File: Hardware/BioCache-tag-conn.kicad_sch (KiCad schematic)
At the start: 36 parts, among them J1 Conn_01x16_Male, J10 Conn_01x04_Male, J11 Conn_01x05_Male, J12 Conn_01x04_Male, J13 Conn_01x01_Male, J14 Conn_01x02_Male, J15 Conn_01x01_Male, J16 Conn_01x01_Male, J17 Conn_01x01_Male, J18 Conn_01x01_Male, J19 Conn_01x02_Male, J2 Conn_01x16_Male, J20 Conn_01x02_Male, J21 Conn_01x02_Male, J22 Conn_01x01_Male, J23 Conn_01x01_Male, J24 Conn_01x01_Male, J25 Conn_01x01_Male, J3 Conn_01x14_Male, J4 Conn_01x14_Male, J5 Conn_01x04_Male, J6 Conn_01x05_Male, J7 Conn_01x05_Male, J8 Conn_01x04_Male, J9 Conn_01x05_Male, U9 61C1024

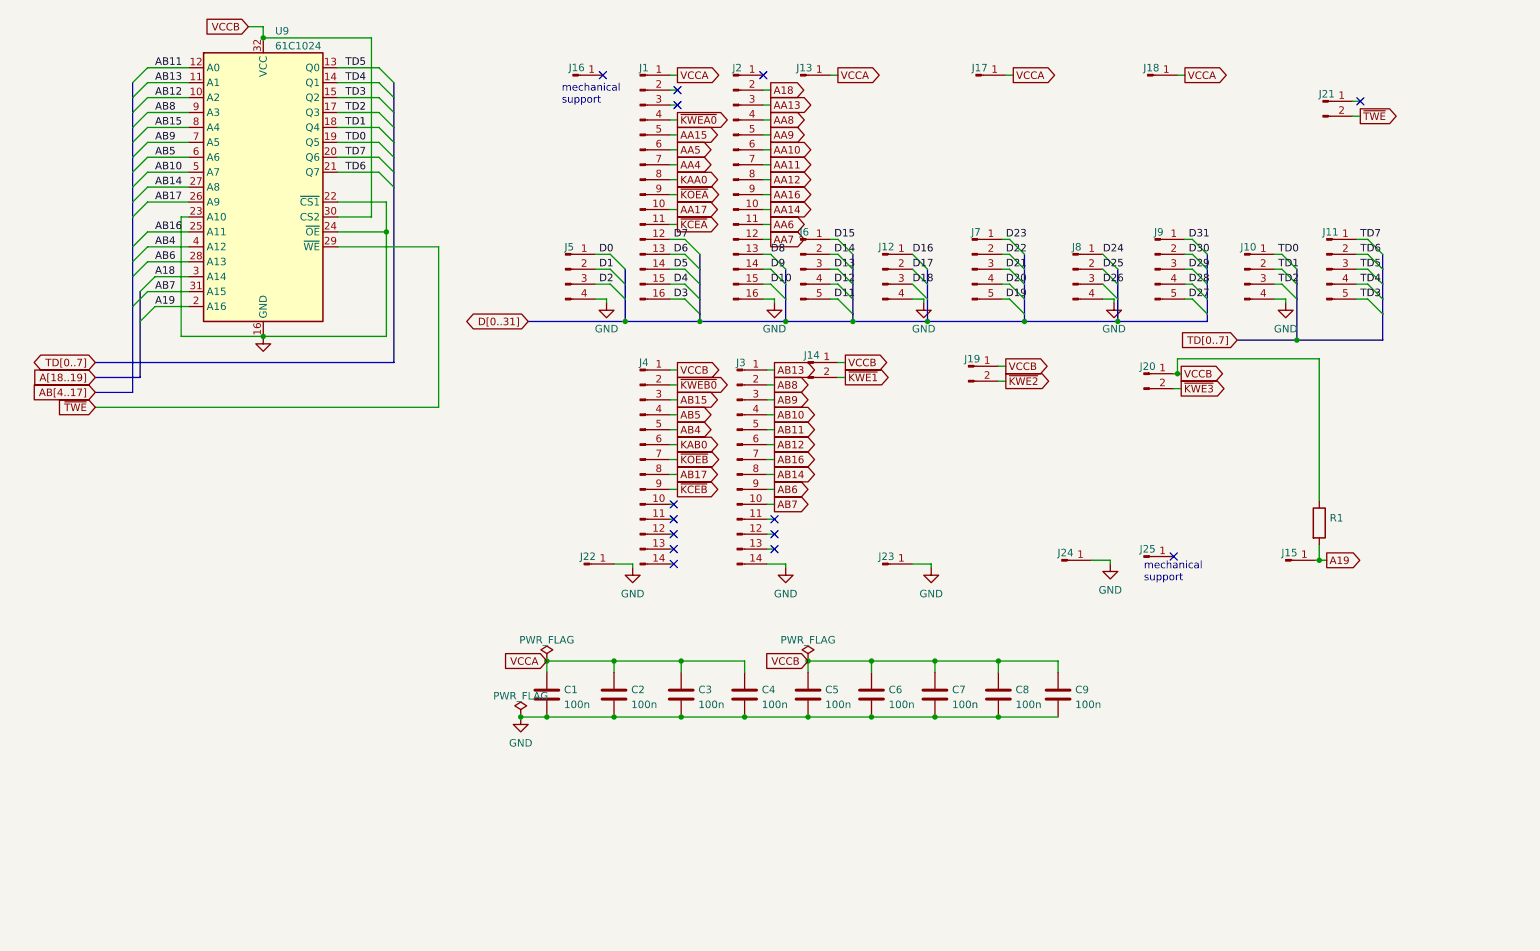
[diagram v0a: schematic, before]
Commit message: Upgrade to KiCad 9, clean-up schematics, set up KiBot
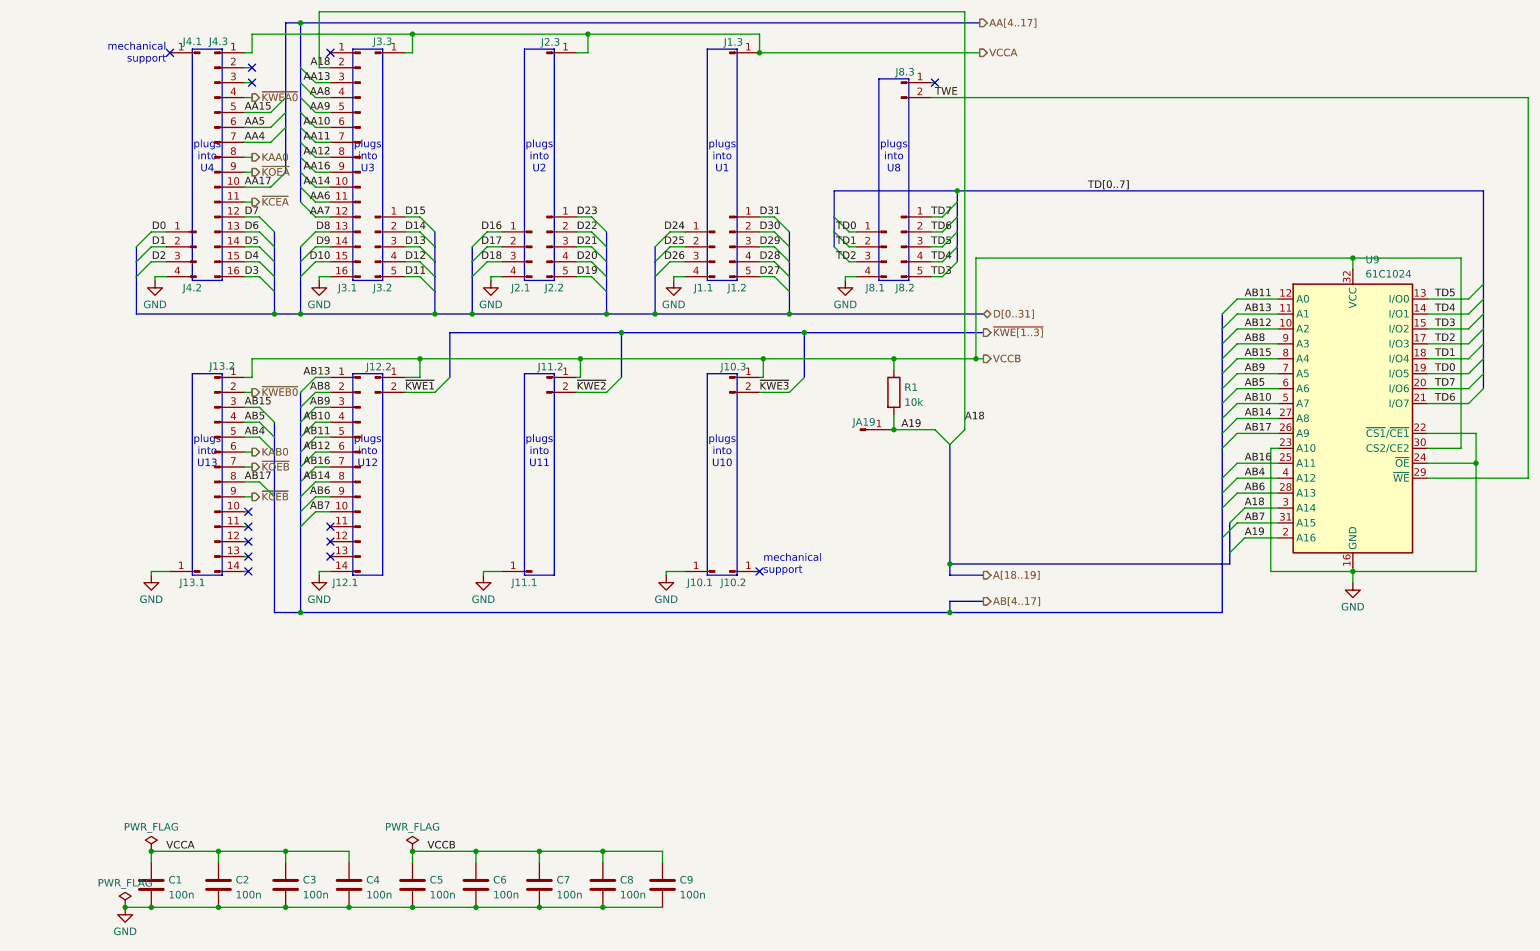
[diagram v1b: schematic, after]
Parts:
- J1.1: renamed from J8; footprint Connector_PinHeader_2.54mm:PinHeader_1x04_P2.54mm_Vertical -> ConnectorNoSquare1:PinHeader_1x04_P2.54mm_Vertical_NoSquare1; symbol Connector:Conn_01x04_Male -> Connector:Conn_01x04_Pin
- J1.2: renamed from J9; footprint Connector_PinHeader_2.54mm:PinHeader_1x05_P2.54mm_Vertical -> ConnectorNoSquare1:PinHeader_1x05_P2.54mm_Vertical_NoSquare1; symbol Connector:Conn_01x05_Male -> Connector:Conn_01x05_Pin
- J1.3: renamed from J18; footprint Connector_PinHeader_2.54mm:PinHeader_1x01_P2.54mm_Vertical -> ConnectorNoSquare1:PinHeader_1x01_P2.54mm_Vertical_NoSquare1; symbol Connector:Conn_01x01_Male -> Connector:Conn_01x01_Pin
- J10.1: renamed from J24; footprint Connector_PinHeader_2.54mm:PinHeader_1x01_P2.54mm_Vertical -> ConnectorNoSquare1:PinHeader_1x01_P2.54mm_Vertical_NoSquare1; symbol Connector:Conn_01x01_Male -> Connector:Conn_01x01_Pin
- J10.2: renamed from J25; footprint Connector_PinHeader_2.54mm:PinHeader_1x01_P2.54mm_Vertical -> ConnectorNoSquare1:PinHeader_1x01_P2.54mm_Vertical_NoSquare1; symbol Connector:Conn_01x01_Male -> Connector:Conn_01x01_Pin
- J10.3: renamed from J20; footprint Connector_PinHeader_2.54mm:PinHeader_1x02_P2.54mm_Vertical -> ConnectorNoSquare1:PinHeader_1x02_P2.54mm_Vertical_NoSquare1; symbol Connector:Conn_01x02_Male -> Connector:Conn_01x02_Pin
- J11.1: renamed from J23; footprint Connector_PinHeader_2.54mm:PinHeader_1x01_P2.54mm_Vertical -> ConnectorNoSquare1:PinHeader_1x01_P2.54mm_Vertical_NoSquare1; symbol Connector:Conn_01x01_Male -> Connector:Conn_01x01_Pin
- J11.2: renamed from J19; footprint Connector_PinHeader_2.54mm:PinHeader_1x02_P2.54mm_Vertical -> ConnectorNoSquare1:PinHeader_1x02_P2.54mm_Vertical_NoSquare1; symbol Connector:Conn_01x02_Male -> Connector:Conn_01x02_Pin
- J12.1: renamed from J3; footprint Connector_PinHeader_2.54mm:PinHeader_1x14_P2.54mm_Vertical -> ConnectorNoSquare1:PinHeader_1x14_P2.54mm_Vertical_NoSquare1; symbol Connector:Conn_01x14_Male -> Connector:Conn_01x14_Pin
- J12.2: renamed from J14; footprint Connector_PinHeader_2.54mm:PinHeader_1x02_P2.54mm_Vertical -> ConnectorNoSquare1:PinHeader_1x02_P2.54mm_Vertical_NoSquare1; symbol Connector:Conn_01x02_Male -> Connector:Conn_01x02_Pin
- J13.1: renamed from J22; footprint Connector_PinHeader_2.54mm:PinHeader_1x01_P2.54mm_Vertical -> ConnectorNoSquare1:PinHeader_1x01_P2.54mm_Vertical_NoSquare1; symbol Connector:Conn_01x01_Male -> Connector:Conn_01x01_Pin
- J13.2: renamed from J4; footprint Connector_PinHeader_2.54mm:PinHeader_1x14_P2.54mm_Vertical -> ConnectorNoSquare1:PinHeader_1x14_P2.54mm_Vertical_NoSquare1; symbol Connector:Conn_01x14_Male -> Connector:Conn_01x14_Pin
- J2.1: renamed from J12; footprint Connector_PinHeader_2.54mm:PinHeader_1x04_P2.54mm_Vertical -> ConnectorNoSquare1:PinHeader_1x04_P2.54mm_Vertical_NoSquare1; symbol Connector:Conn_01x04_Male -> Connector:Conn_01x04_Pin
- J2.2: renamed from J7; footprint Connector_PinHeader_2.54mm:PinHeader_1x05_P2.54mm_Vertical -> ConnectorNoSquare1:PinHeader_1x05_P2.54mm_Vertical_NoSquare1; symbol Connector:Conn_01x05_Male -> Connector:Conn_01x05_Pin
- J2.3: renamed from J17; footprint Connector_PinHeader_2.54mm:PinHeader_1x01_P2.54mm_Vertical -> ConnectorNoSquare1:PinHeader_1x01_P2.54mm_Vertical_NoSquare1; symbol Connector:Conn_01x01_Male -> Connector:Conn_01x01_Pin
- J3.1: renamed from J2; footprint Connector_PinHeader_2.54mm:PinHeader_1x16_P2.54mm_Vertical -> ConnectorNoSquare1:PinHeader_1x16_P2.54mm_Vertical_NoSquare1; symbol Connector:Conn_01x16_Male -> Connector:Conn_01x16_Pin
- J3.2: renamed from J6; footprint Connector_PinHeader_2.54mm:PinHeader_1x05_P2.54mm_Vertical -> ConnectorNoSquare1:PinHeader_1x05_P2.54mm_Vertical_NoSquare1; symbol Connector:Conn_01x05_Male -> Connector:Conn_01x05_Pin
- J3.3: renamed from J13; footprint Connector_PinHeader_2.54mm:PinHeader_1x01_P2.54mm_Vertical -> ConnectorNoSquare1:PinHeader_1x01_P2.54mm_Vertical_NoSquare1; symbol Connector:Conn_01x01_Male -> Connector:Conn_01x01_Pin
- J4.1: renamed from J16; footprint Connector_PinHeader_2.54mm:PinHeader_1x01_P2.54mm_Vertical -> ConnectorNoSquare1:PinHeader_1x01_P2.54mm_Vertical_NoSquare1; symbol Connector:Conn_01x01_Male -> Connector:Conn_01x01_Pin
- J4.2: renamed from J5; footprint Connector_PinHeader_2.54mm:PinHeader_1x04_P2.54mm_Vertical -> ConnectorNoSquare1:PinHeader_1x04_P2.54mm_Vertical_NoSquare1; symbol Connector:Conn_01x04_Male -> Connector:Conn_01x04_Pin
- J4.3: renamed from J1; footprint Connector_PinHeader_2.54mm:PinHeader_1x16_P2.54mm_Vertical -> ConnectorNoSquare1:PinHeader_1x16_P2.54mm_Vertical_NoSquare1; symbol Connector:Conn_01x16_Male -> Connector:Conn_01x16_Pin
- J8.1: renamed from J10; footprint Connector_PinHeader_2.54mm:PinHeader_1x04_P2.54mm_Vertical -> ConnectorNoSquare1:PinHeader_1x04_P2.54mm_Vertical_NoSquare1; symbol Connector:Conn_01x04_Male -> Connector:Conn_01x04_Pin
- J8.2: renamed from J11; footprint Connector_PinHeader_2.54mm:PinHeader_1x05_P2.54mm_Vertical -> ConnectorNoSquare1:PinHeader_1x05_P2.54mm_Vertical_NoSquare1; symbol Connector:Conn_01x05_Male -> Connector:Conn_01x05_Pin
- J8.3: renamed from J21; footprint Connector_PinHeader_2.54mm:PinHeader_1x02_P2.54mm_Vertical -> ConnectorNoSquare1:PinHeader_1x02_P2.54mm_Vertical_NoSquare1; symbol Connector:Conn_01x02_Male -> Connector:Conn_01x02_Pin
- JA19: renamed from J15; symbol Connector:Conn_01x01_Male -> Connector:Conn_01x01_Pin
- R1: value (none) -> 10k; footprint (none) -> Resistor_SMD:R_0805_2012Metric_Pad1.20x1.40mm_HandSolder
- U9: symbol Memory_RAM:628128_DIP32_SSOP32 -> SOJmem:IS6xC1024AL-xxJ
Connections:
- net ~{TWE} renamed TWE
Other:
- note added: "plugs into U1"
- note added: "plugs into U10"
- note added: "plugs into U11"
- note added: "plugs into U12"
- note added: "plugs into U13"
- note added: "plugs into U2"
- note added: "plugs into U3"
- note added: "plugs into U4"
- note added: "plugs into U8"
- title: (none) -> Biostar MB-84xx-UUD 1MB cache tag and connectors
- moved on the sheet: C1, C2, C3, C4, C5, C6, C7, C8, C9, J1.1, J1.2, J1.3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

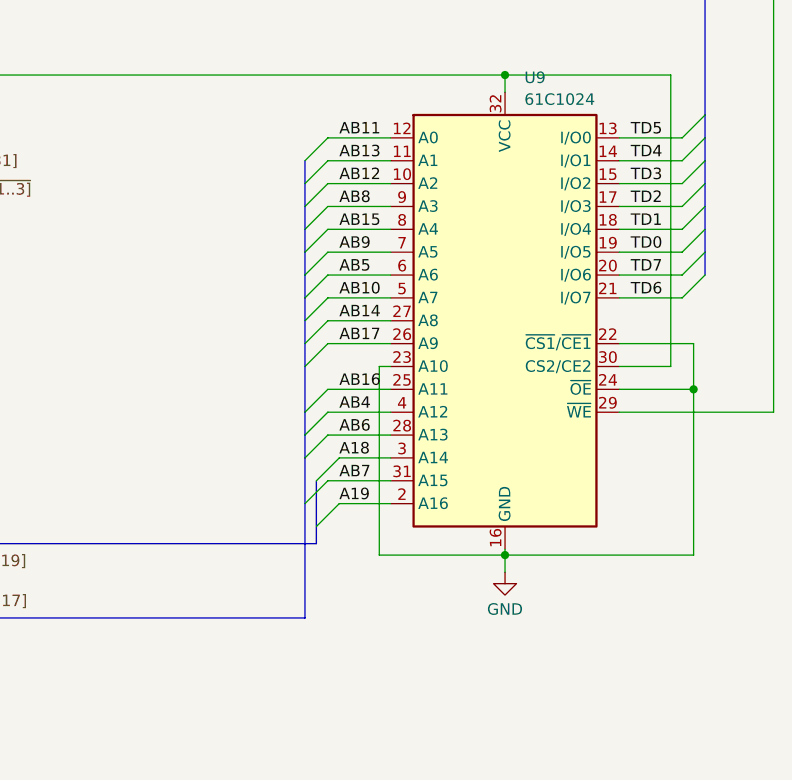
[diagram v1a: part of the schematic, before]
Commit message: Re-Route U9 (TAG ram) to support 32K*8 and 64K*8
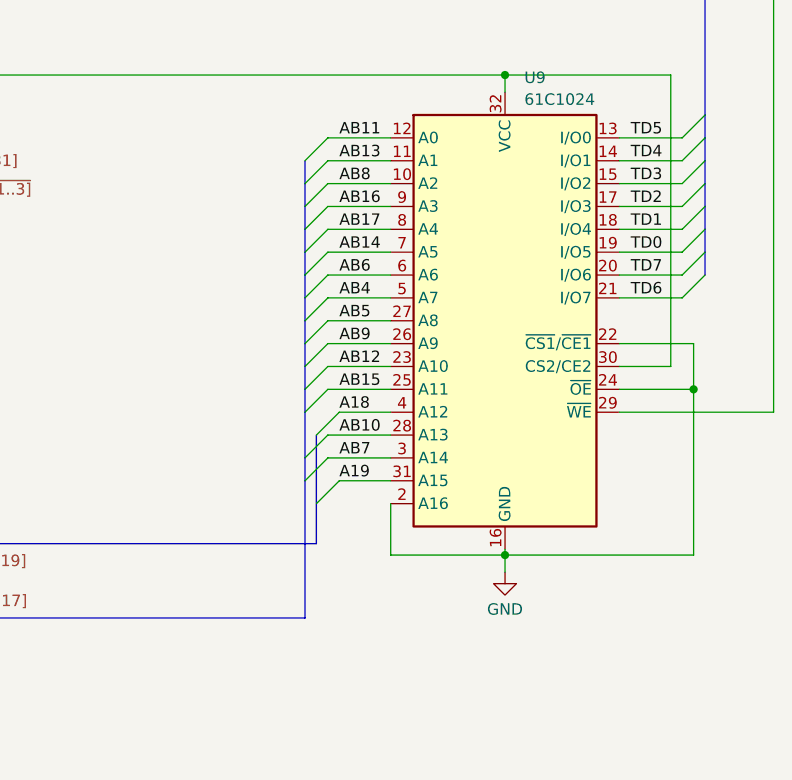
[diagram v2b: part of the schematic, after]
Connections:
- net A18: now also U9.4 (A12); no longer U9.3 (A14)
- net A19: now also U9.31 (A15); no longer U9.2 (A16)
- net AB10: now also U9.28 (A13); no longer U9.5 (A7)
- net AB12: now also U9.23 (A10); no longer U9.10 (A2)
- net AB14: now also U9.7 (A5); no longer U9.27 (A8)
- net AB15: now also U9.25 (A11); no longer U9.8 (A4)
- net AB16: now also U9.9 (A3); no longer U9.25 (A11)
- net AB17: now also U9.8 (A4); no longer U9.26 (A9)
- net AB4: now also U9.5 (A7); no longer U9.4 (A12)
- net AB5: now also U9.27 (A8); no longer U9.6 (A6)
- net AB6: now also U9.6 (A6); no longer U9.28 (A13)
- net AB7: now also U9.3 (A14); no longer U9.31 (A15)
- net AB8: now also U9.10 (A2); no longer U9.9 (A3)
- net AB9: now also U9.26 (A9); no longer U9.7 (A5)
- net GND: now also U9.2 (A16); no longer U9.23 (A10)

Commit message: Remove custom definition of SOJ32 memory chip
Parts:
- U9: footprint Package_SOJ:SOJ-32_7.58x20.955mm_P1.27mm -> Package_SO:SOJ-32_7.62x20.955mm_P1.27mm; symbol SOJmem:IS6xC1024AL-xxJ -> Memory_RAM:IS6xC1024AL-xxJ
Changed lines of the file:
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@@
 	)
 	(symbol
-		(lib_id "SOJmem:IS6xC1024AL-xxJ")
+		(lib_id "Memory_RAM:IS6xC1024AL-xxJ")
 		(at 238.76 81.915 0)
 		(unit 1)
@@
 			)
 		)
-		(property "Footprint" "Package_SOJ:SOJ-32_7.58x20.955mm_P1.27mm"
+		(property "Footprint" "Package_SO:SOJ-32_7.62x20.955mm_P1.27mm"
 			(at 238.76 81.915 0)
 			(effects
